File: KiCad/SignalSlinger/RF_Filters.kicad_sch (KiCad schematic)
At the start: 11 parts, among them J301 To Antenna

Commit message: BOM Corrections
o Updated BOM
o Updated Footprints
o Updated PCB and Gerbers
o Updated schematic
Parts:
- C302, C305: Digi-Key Part No. (none) -> GRM2195C2A112JA01D-ND
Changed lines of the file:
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@@
   (title_block
     (title "SignalSlinger")
-    (date "2024-06-12")
-    (rev "3.3")
+    (date "2024-06-13")
+    (rev "3.4")
   )
   (junction (at 165.1 83.82) (diameter 0) (color 0 0 0 0)
@@
     (pin "2")
   )
+  (symbol (lib_id "Device:C_Small") (at 160.02 88.9 0) (unit 1)
+    (in_bom yes) (on_board yes)
+    (property "Reference" "C305" (id 0) (at 160.274 87.122 0)
+      (effects (font (size 1.27 1.27)) (justify left))
+    )
+    (property "Value" "1100pF" (id 1) (at 160.274 90.932 0)
+      (effects (font (size 1.27 1.27)) (justify left))
+    )
+    (property "Footprint" "Capacitor_SMD:C_0805_2012Metric" (id 2) (at 160.02 88.9 0)
+      (effects (font (size 1.27 1.27)) hide)
+    )
+    (property "Datasheet" "" (id 3) (at 160.02 88.9 0))
+    (property "Manufacturer" "Murata Electronics" (id 6) (at 160.02 88.9 0)
+      (effects (font (size 1.27 1.27)) hide)
+    )
+    (property "Manufacturer PN" "GRM2195C2A112JA01D" (id 7) (at 160.02 88.9 0)
+      (effects (font (size 1.27 1.27)) hide)
+    )
+    (property "Description" "1100 pF ±5% 100V Ceramic Capacitor C0G, NP0 0805 (2012 Metric)" (id 8) (at 160.02 88.9 0)
+      (effects (font (size 1.27 1.27)) hide)
+    )
+    (property "Digi-Key Part No." "GRM2195C2A112JA01D-ND" (id 9) (at 160.02 88.9 0)
+      (effects (font (size 1.27 1.27)) hide)
+    )
+    (pin "1")
+    (pin "2")
+  )
   (symbol (lib_id "Device:INDUCTOR_SMALL") (at 151.13 83.82 0) (unit 1)
     (in_bom yes) (on_board yes)
@@
     (pin "2")
   )
-  (symbol (lib_id "Device:C_Small") (at 160.02 88.9 0) (unit 1)
-    (in_bom yes) (on_board yes)
-    (property "Reference" "C305" (id 0) (at 160.274 87.122 0)
-      (effects (font (size 1.27 1.27)) (justify left))
-    )
-    (property "Value" "1100pF" (id 1) (at 160.274 90.932 0)
-      (effects (font (size 1.27 1.27)) (justify left))
-    )
-    (property "Footprint" "Capacitor_SMD:C_0805_2012Metric" (id 2) (at 160.02 88.9 0)
-      (effects (font (size 1.27 1.27)) hide)
-    )
-    (property "Datasheet" "" (id 3) (at 160.02 88.9 0))
-    (property "Manufacturer" "Murata Electronics" (id 6) (at 160.02 88.9 0)
-      (effects (font (size 1.27 1.27)) hide)
-    )
-    (property "Manufacturer PN" "GRM2195C2A112JA01D" (id 7) (at 160.02 88.9 0)
-      (effects (font (size 1.27 1.27)) hide)
-    )
-    (property "Description" "Multilayer Ceramic Capacitors MLCC - SMD/SMT 1100 pF 100 VDC 5% 0805 C0G (NP0)" (id 8) (at 160.02 88.9 0)
-      (effects (font (size 1.27 1.27)) hide)
-    )
-    (pin "1")
-    (pin "2")
-  )
   (symbol (lib_id "power:GND") (at 160.02 91.44 0) (unit 1)
     (in_bom yes) (on_board yes) (fields_autoplaced)
@@
       (effects (font (size 1.27 1.27)) hide)
     )
-    (property "Description" "Multilayer Ceramic Capacitors MLCC - SMD/SMT 1100 pF 100 VDC 5% 0805 C0G (NP0)" (id 8) (at 116.84 88.9 0)
-      (effects (font (size 1.27 1.27)) hide)
-    )
+    (property "Description" "1100 pF ±5% 100V Ceramic Capacitor C0G, NP0 0805 (2012 Metric)" (id 8) (at 116.84 88.9 0)
+      (effects (font (size 1.27 1.27)) hide)
+    )
+    (property "Digi-Key Part No." "GRM2195C2A112JA01D-ND" (id 9) (at 116.84 88.9 0)
+      (effects (font (size 1.27 1.27)) hide)
+    )

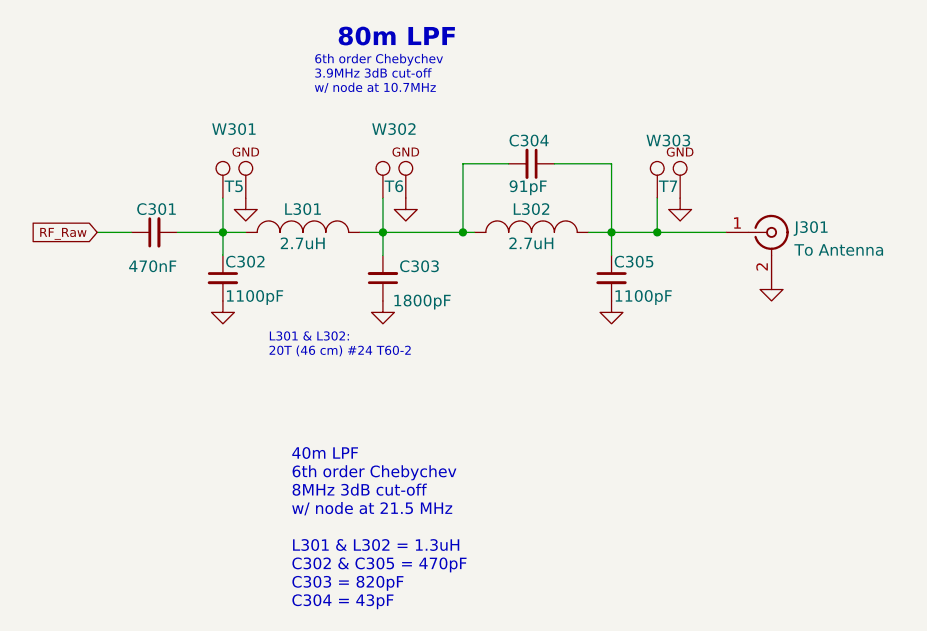
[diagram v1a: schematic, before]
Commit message: Design Updates
oThe boost regulator was removed from the design.
oAn additional load switch was added to the design.
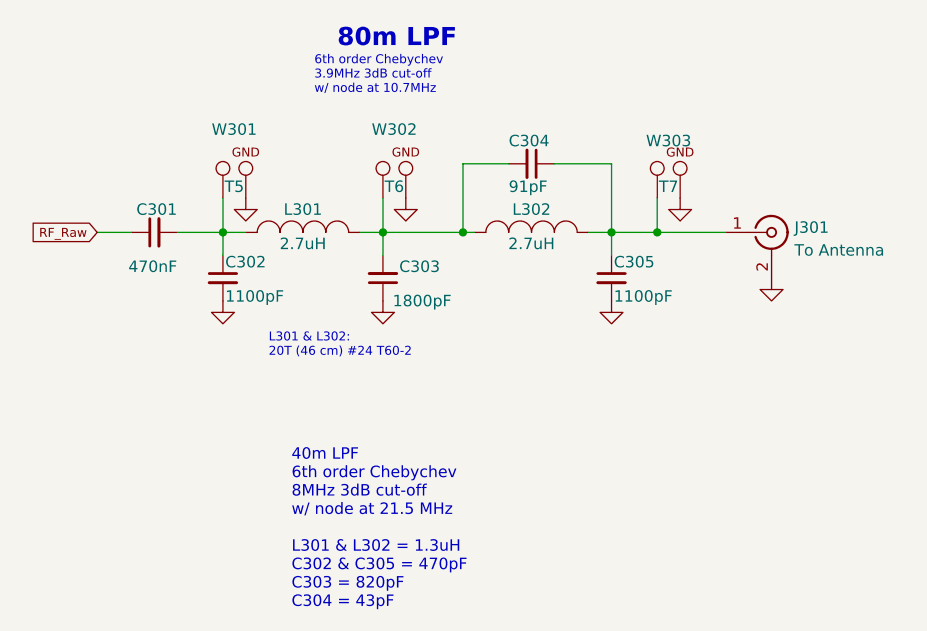
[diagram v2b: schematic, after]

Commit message: Production Updates
Corrects copper spacing issues
Removes warnings
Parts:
- J301: symbol Connector:Conn_Coaxial -> SignalSlinger Library:Conn_Coaxial
- L301, L302: footprint Inductors:Toroid_T-60_2TH_Vertical -> SignalSlinger_Footprints:Toroid_T-60_2TH_Vertical; symbol Device:INDUCTOR_SMALL -> SignalSlinger Library:INDUCTOR_SMALL
- W301, W302, W303: footprint Measurement:Measurement_Point_ScopeProbe_Round-SMD-2sides-Pad_Small -> SignalSlinger_Footprints:Measurement_Point_ScopeProbe_Round-SMD-2sides-Pad_Small; symbol Connector:TEST_SCOPE -> SignalSlinger Library:TEST_SCOPE

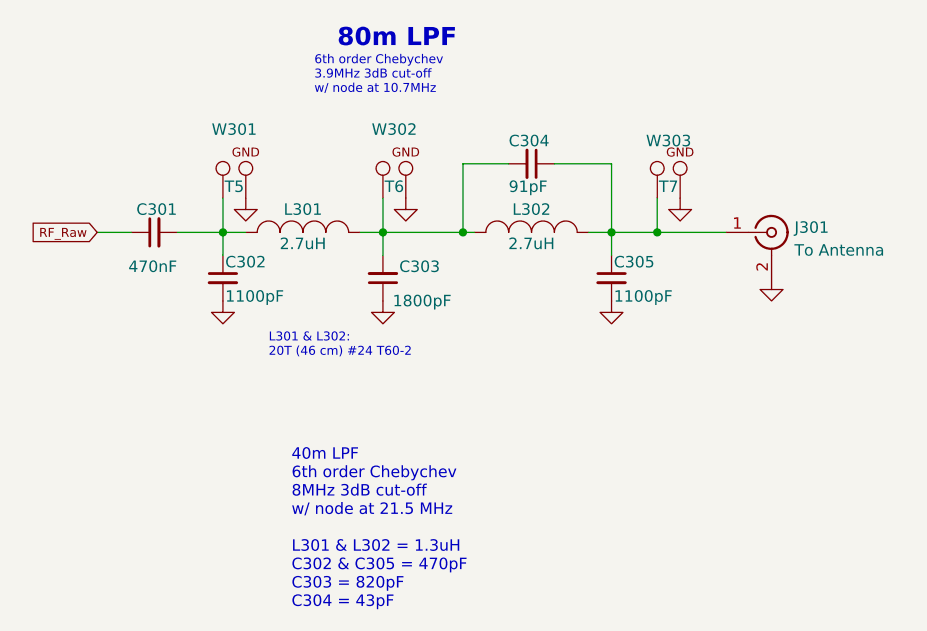
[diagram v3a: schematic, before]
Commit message: Restoring Old KiCad Design
Restoring prototype HW design
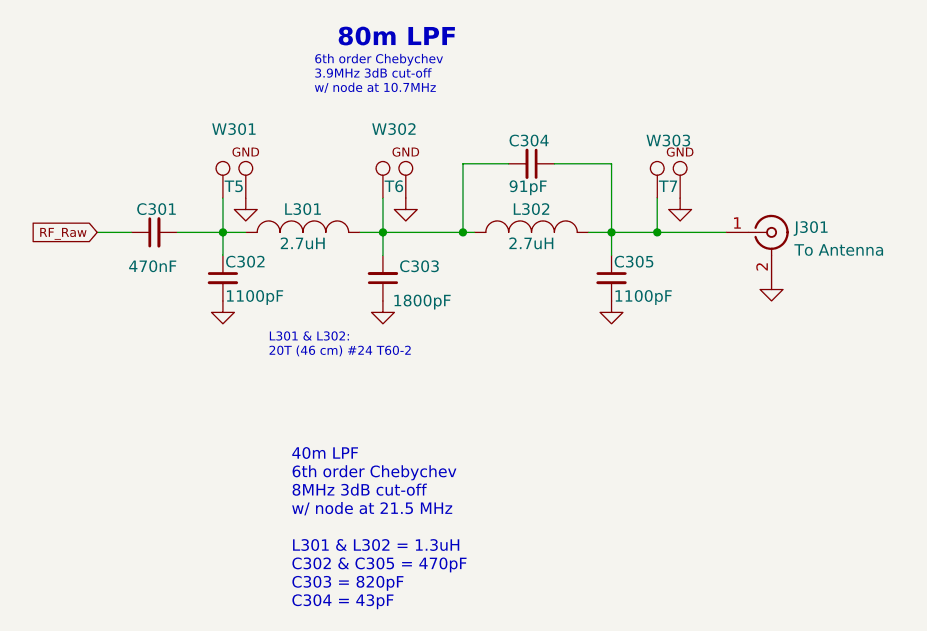
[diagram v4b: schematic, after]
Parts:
- J301: symbol SignalSlinger Library:Conn_Coaxial -> Connector:Conn_Coaxial
- L301, L302: footprint SignalSlinger_Footprints:Toroid_T-60_2TH_Vertical -> Inductors:Toroid_T-60_2TH_Vertical; symbol SignalSlinger Library:INDUCTOR_SMALL -> Device:INDUCTOR_SMALL
- W301, W302, W303: footprint SignalSlinger_Footprints:Measurement_Point_ScopeProbe_Round-SMD-2sides-Pad_Small -> Measurement:Measurement_Point_ScopeProbe_Round-SMD-2sides-Pad_Small; symbol SignalSlinger Library:TEST_SCOPE -> Connector:TEST_SCOPE

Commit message: Updated to Latest KiCad Version
Updated files
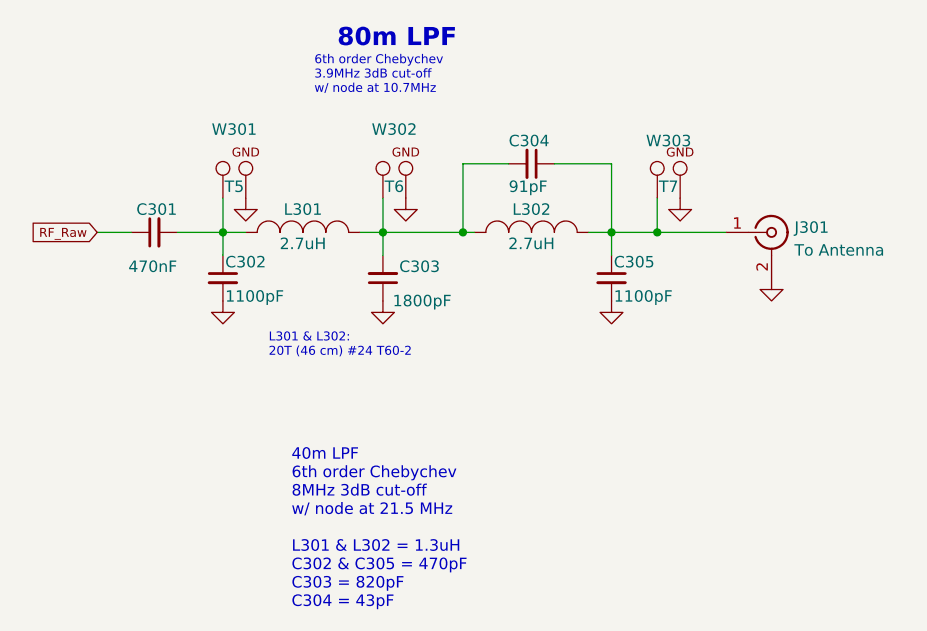
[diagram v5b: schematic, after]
